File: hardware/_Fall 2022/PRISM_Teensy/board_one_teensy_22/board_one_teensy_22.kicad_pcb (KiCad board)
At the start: 2 copper layers, 15 parts, among them J1 EAST, J2 CORE_IO, J3 USB_micro, U1 Teensy4.1, U2 BNO055_Breakout, U3 3966

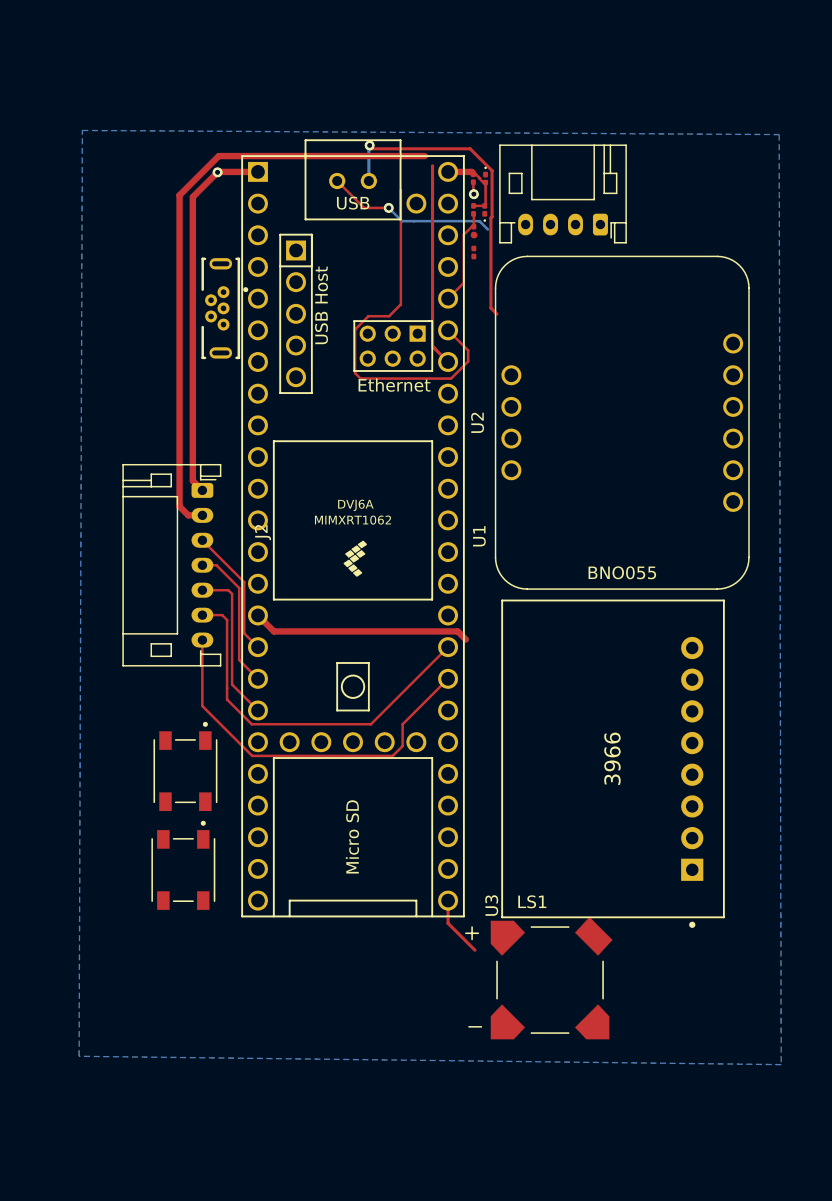
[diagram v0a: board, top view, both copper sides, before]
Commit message: Fix errors on TX/RX and added buzzer
Current state: Board 1 - need to check diodes; Board 4 - done; GPS- not showing layout traces, all need logos
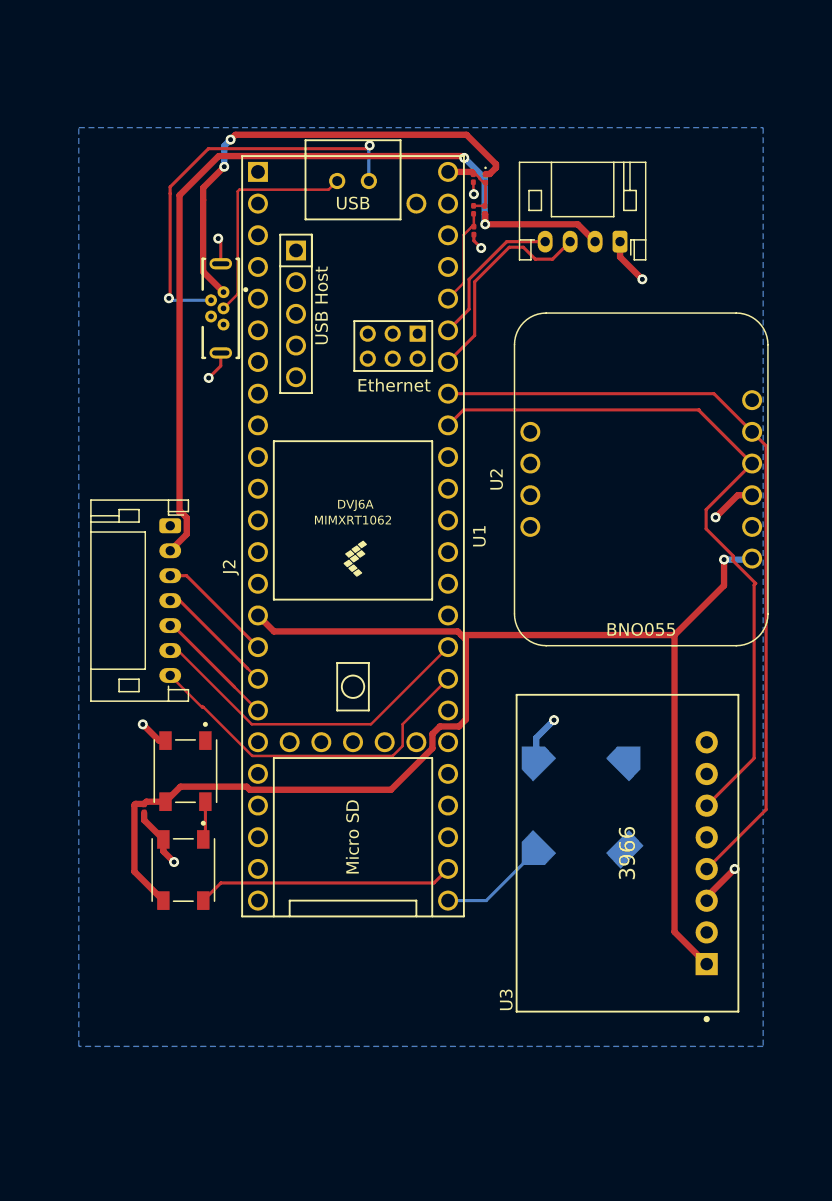
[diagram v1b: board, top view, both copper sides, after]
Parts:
- LS1: moved to B.Cu
- moved C2 51.8 mm to (115.7, 111.2), turned to 90 degrees
- moved LS1 14.2 mm to (150.8, 111.0)
- moved U3 7.65 mm to (154.5, 114.8)
- moved U2 4.79 mm to (155.6, 84.8)
- moved J2 3.83 mm to (117.8, 88.6)
- moved J1 2.08 mm to (153.9, 65.8)
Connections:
- C2 pad 2: +3.3V -> /3.3V
- D4 pad 3: +3.3V -> /3.3V
- D5 pad 3: +3.3V -> /3.3V
- U1 pad 42: /RX 0 -> /TX 0
- U1 pad 43: /TX 0 -> /RX 0
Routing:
- net /3.3V: track 17.5 -> 117.3 mm, vias 0 -> 1
- net /SCL 0: track 0.00 -> 63.1 mm
- net /SDA 0: track 0.00 -> 58.9 mm
- net /V_USB: track 0.00 -> 37.6 mm, vias 0 -> 2
- net /V_BATT: track 48.1 -> 69.8 mm, vias 0 -> 2
- net /NEOPIXEL: track 0.00 -> 20.7 mm
- net /TX 0: track 30.2 -> 17.1 mm
- net Net-(J3-Pad2): track 25.4 -> 32.9 mm, vias 1 -> 2
- net GND: track 30.9 -> 24.3 mm, vias 2 -> 8
- net Net-(J3-Pad3): track 13.7 -> 18.7 mm, vias 1 -> 0
- net unconnected-(J3-PadS1): track 0.00 -> 4.51 mm, vias 0 -> 2
- net /RX 0: track 16.2 -> 12.1 mm
- net /BUZZER: track 4.87 -> 8.72 mm
- net Net-(D4-Pad1): track 0.00 -> 3.10 mm
- net /ARM: track 12.7 -> 10.1 mm
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
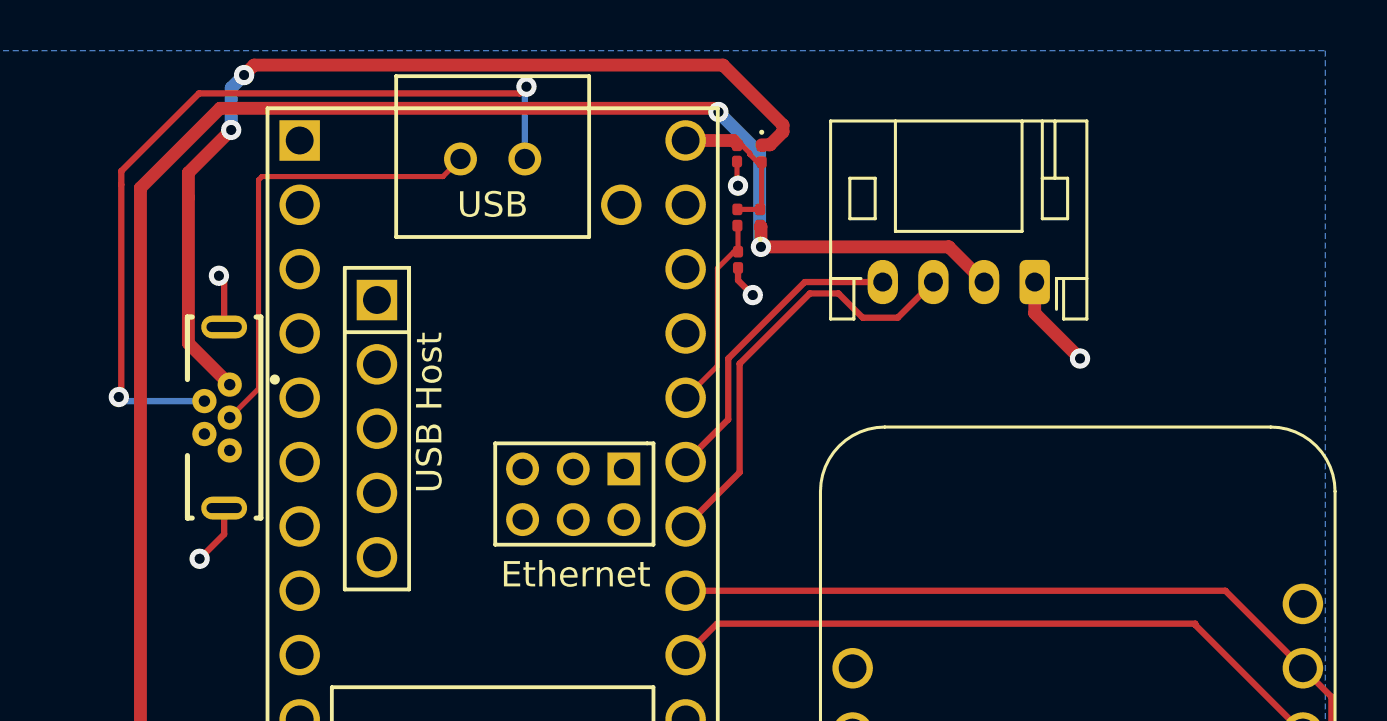
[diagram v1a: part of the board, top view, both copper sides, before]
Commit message: Add schottcky diodes to main teensy
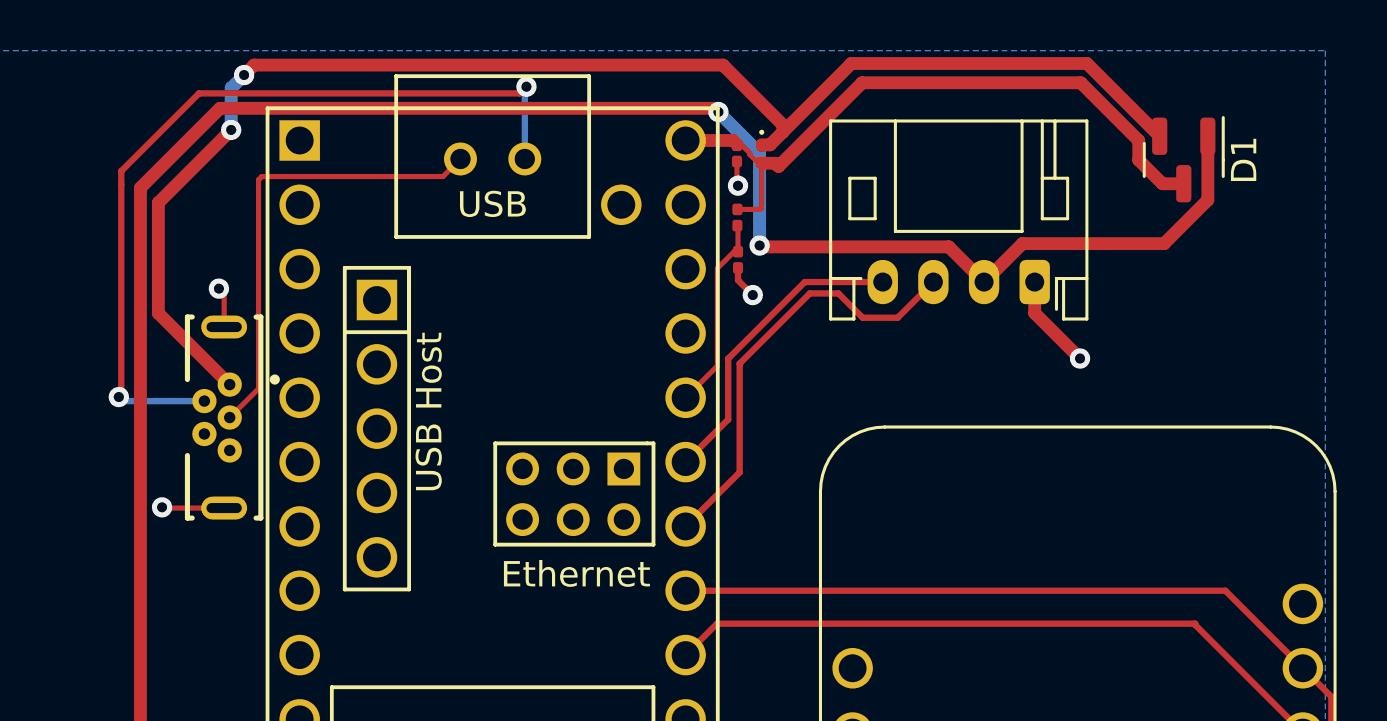
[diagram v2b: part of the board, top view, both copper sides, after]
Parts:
- D1: value DIODE -> BAT54C; footprint Diode_SMD:D_0201_0603Metric -> Package_TO_SOT_SMD:SOT-23
- R4: value 100K -> 200K
- moved D1 16.9 mm to (159.8, 61.0), turned to -90 degrees
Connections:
- D1 pad 2: /VIN -> /V_USB
- J3 pad S1: unconnected-(J3-PadS1) -> GND
- J3 pad S2: unconnected-(J3-PadS1) -> GND
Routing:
- net /VIN: track 6.16 -> 26.3 mm
- net /V_USB: track 37.6 -> 55.7 mm
- net /V_BATT: track 69.8 -> 81.7 mm
- net unconnected-(J3-PadS1): track 4.51 -> 0.00 mm, vias 2 -> 0
- net GND: track 24.3 -> 28.4 mm, vias 8 -> 10

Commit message: logos
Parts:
- added ?: LOGO, LOGO, F.Cu at (137.5, 53.6)
- added ?: LOGO, LOGO, F.Cu at (138.4, 134.6)
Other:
- board outline added: 61 x 88.9 mm

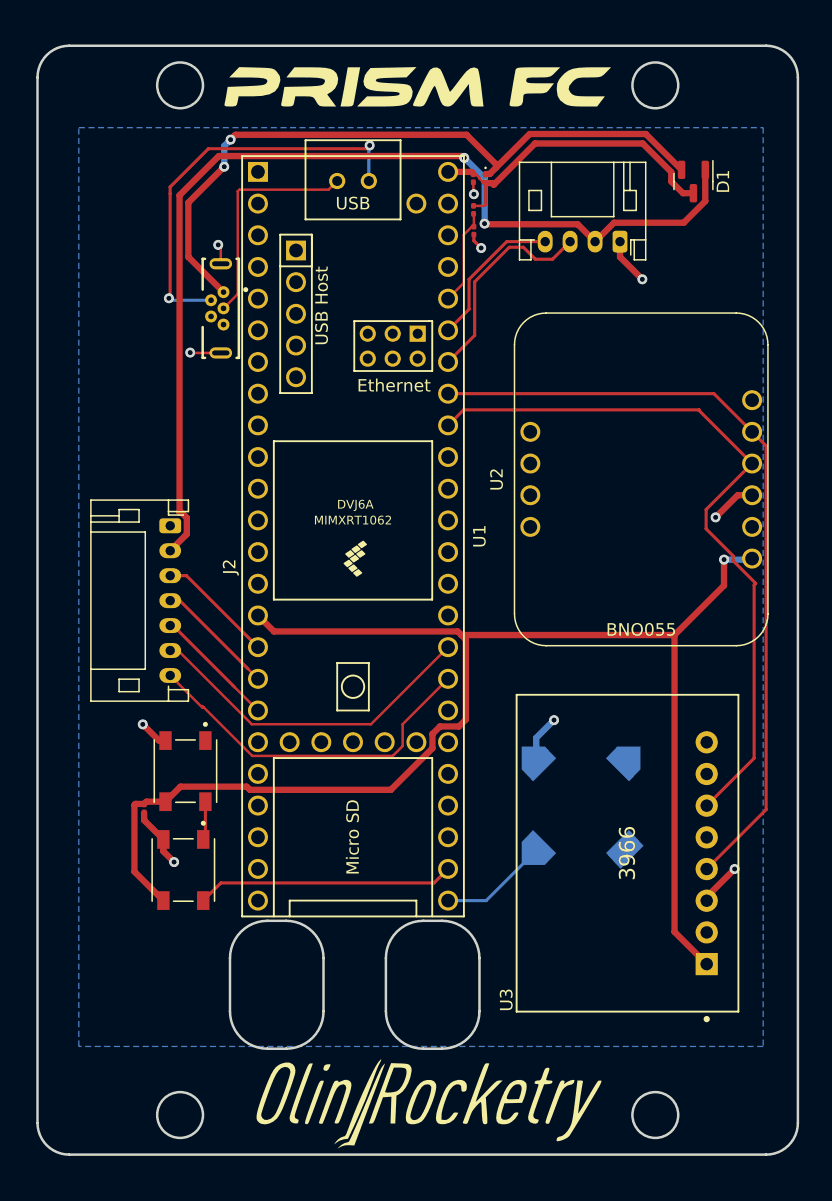
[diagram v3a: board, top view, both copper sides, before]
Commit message: Completed IO layout, added board 1 plated holes
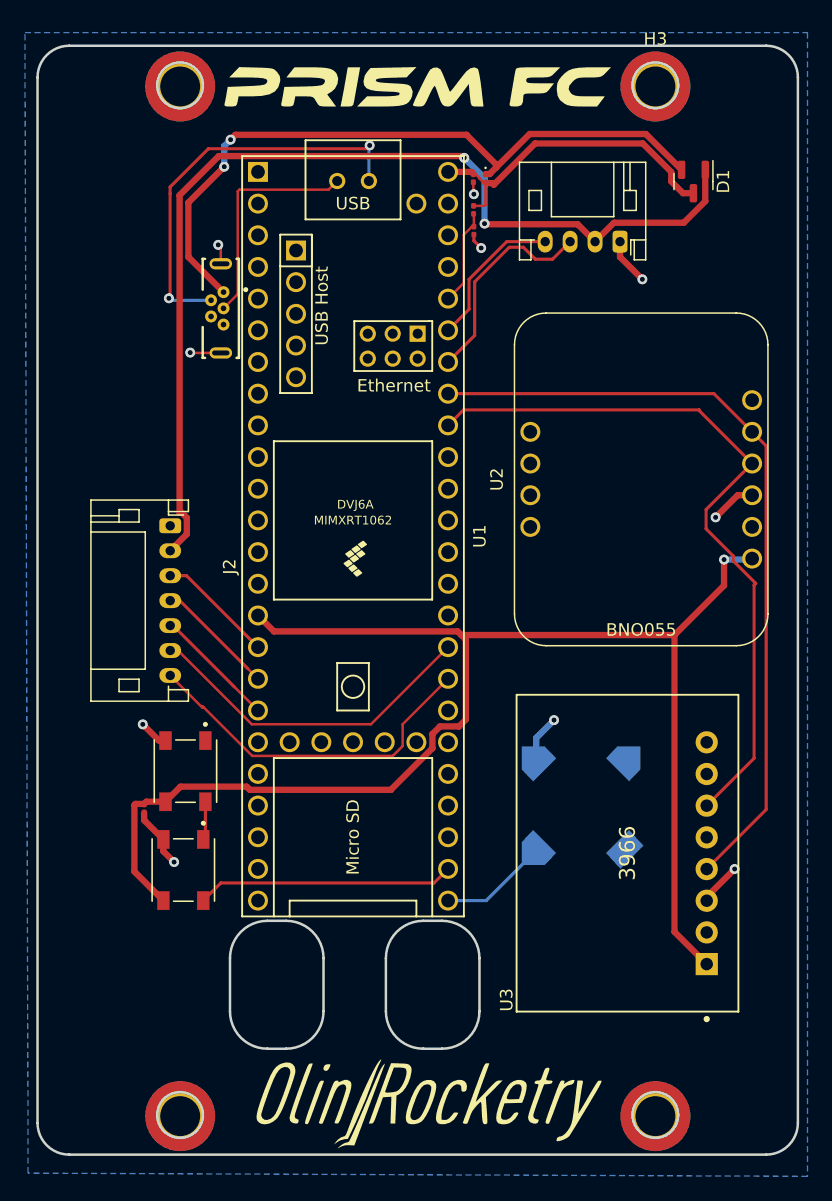
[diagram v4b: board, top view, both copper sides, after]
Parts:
- added H1: MountingHole_Pad, MountingHole:MountingHole_3.2mm_M3_DIN965_Pad_TopBottom, F.Cu at (118.6, 53.3)
- added H2: MountingHole, MountingHole:MountingHole_3.2mm_M3_DIN965_Pad_TopBottom, F.Cu at (156.7, 135.9)
- added H3: MountingHole, MountingHole:MountingHole_3.2mm_M3_DIN965_Pad_TopBottom, F.Cu at (156.7, 53.3)
- added H4: MountingHole, MountingHole:MountingHole_3.2mm_M3_DIN965_Pad_TopBottom, F.Cu at (118.6, 135.9)
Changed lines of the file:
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@@
     )
+  )
+  (footprint "MountingHole:MountingHole_3.2mm_M3_DIN965_Pad_TopBottom" (layer "F.Cu")
+    (at 118.618 53.34)
+    (descr "Mounting Hole 3.2mm, M3, DIN965")
+    (tags "mounting hole 3.2mm m3 din965")
+    (property "Sheetfile" "CoreIO.kicad_sch")
+    (property "Sheetname" "")
+    (attr exclude_from_pos_files)
+    (fp_text reference "H1" (at 0 -3.8) (layer "User.1")
+      (effects (font (size 1 1) (thickness 0.15)))
+    )
+    (fp_text value "MountingHole_Pad" (at 0 3.8) (layer "F.Fab")
+      (effects (font (size 1 1) (thickness 0.15)))
+    )
+    (fp_text user "${REFERENCE}" (at 0 0) (layer "F.Fab")
+      (effects (font (size 1 1) (thickness 0.15)))
+    )
+    (fp_circle (center 0 0) (end 2.8 0) (layer "Cmts.User") (width 0.15) (fill none))
+    (fp_circle (center 0 0) (end 3.05 0) (layer "F.CrtYd") (width 0.05) (fill none))
+    (pad "1" thru_hole circle (at 0 0) (size 3.6 3.6) (drill 3.2) (layers *.Cu *.Mask)
+      (pinfunction "1") (pintype "input"))
+    (pad "1" connect circle (at 0 0) (size 5.6 5.6) (layers "F.Cu" "F.Mask")
+      (pinfunction "1") (pintype "input"))
+    (pad "1" connect circle (at 0 0) (size 5.6 5.6) (layers "B.Cu" "B.Mask")
+      (pinfunction "1") (pintype "input"))
   )
   (footprint "neopixel:LED_1655" (layer "F.Cu")
@@
     )
   )
+  (footprint "MountingHole:MountingHole_3.2mm_M3_DIN965_Pad_TopBottom" (layer "F.Cu")
+    (at 118.618 135.89)
+    (descr "Mounting Hole 3.2mm, M3, DIN965")
+    (tags "mounting hole 3.2mm m3 din965")
+    (property "Sheetfile" "CoreIO.kicad_sch")
+    (property "Sheetname" "")
+    (attr exclude_from_pos_files)
+    (fp_text reference "H4" (at 0 -3.8) (layer "User.1")
+      (effects (font (size 1 1) (thickness 0.15)))
+    )
+    (fp_text value "MountingHole" (at 0 3.8) (layer "F.Fab")
+      (effects (font (size 1 1) (thickness 0.15)))
+    )
+    (fp_text user "${REFERENCE}" (at 0 0) (layer "F.Fab")
+      (effects (font (size 1 1) (thickness 0.15)))
+    )
+    (fp_circle (center 0 0) (end 2.8 0) (layer "Cmts.User") (width 0.15) (fill none))
+    (fp_circle (center 0 0) (end 3.05 0) (layer "F.CrtYd") (width 0.05) (fill none))
+    (pad "1" thru_hole circle (at 0 0) (size 3.6 3.6) (drill 3.2) (layers *.Cu *.Mask))
+    (pad "1" connect circle (at 0 0) (size 5.6 5.6) (layers "F.Cu" "F.Mask"))
+    (pad "1" connect circle (at 0 0) (size 5.6 5.6) (layers "B.Cu" "B.Mask"))
+  )
+  (footprint "MountingHole:MountingHole_3.2mm_M3_DIN965_Pad_TopBottom" (layer "F.Cu")
+    (at 156.718 53.34)
+    (descr "Mounting Hole 3.2mm, M3, DIN965")
+    (tags "mounting hole 3.2mm m3 din965")
+    (property "Sheetfile" "CoreIO.kicad_sch")
+    (property "Sheetname" "")
+    (attr exclude_from_pos_files)
+    (fp_text reference "H3" (at 0 -3.8) (layer "F.SilkS")
+      (effects (font (size 1 1) (thickness 0.15)))
+    )
+    (fp_text value "MountingHole" (at 0 3.8) (layer "F.Fab")
+      (effects (font (size 1 1) (thickness 0.15)))
+    )
+    (fp_text user "${REFERENCE}" (at 0 0) (layer "F.Fab")
+      (effects (font (size 1 1) (thickness 0.15)))
+    )
+    (fp_circle (center 0 0) (end 2.8 0) (layer "Cmts.User") (width 0.15) (fill none))
+    (fp_circle (center 0 0) (end 3.05 0) (layer "F.CrtYd") (width 0.05) (fill none))
+    (pad "1" thru_hole circle (at 0 0) (size 3.6 3.6) (drill 3.2) (layers *.Cu *.Mask))
+    (pad "1" connect circle (at 0 0) (size 5.6 5.6) (layers "B.Cu" "B.Mask"))
+    (pad "1" connect circle (at 0 0) (size 5.6 5.6) (layers "F.Cu" "F.Mask"))
+  )
   (footprint "Sensors:BNO055_Breakout" (layer "F.Cu")
     (at 155.58 84.84 90)
@@
       (rotate (xyz -90 0 0))
     )
+  )
+  (footprint "MountingHole:MountingHole_3.2mm_M3_DIN965_Pad_TopBottom" (layer "F.Cu")
+    (at 156.718 135.89)
+    (descr "Mounting Hole 3.2mm, M3, DIN965")
+    (tags "mounting hole 3.2mm m3 din965")
+    (property "Sheetfile" "CoreIO.kicad_sch")
+    (property "Sheetname" "")
+    (attr exclude_from_pos_files)
+    (fp_text reference "H2" (at 0 -3.8) (layer "User.1")
+      (effects (font (size 1 1) (thickness 0.15)))
+    )
+    (fp_text value "MountingHole" (at 0 3.8) (layer "F.Fab")
+      (effects (font (size 1 1) (thickness 0.15)))
+    )
+    (fp_text user "${REFERENCE}" (at 0 0) (layer "F.Fab")
+      (effects (font (size 1 1) (thickness 0.15)))
+    )
+    (fp_circle (center 0 0) (end 2.8 0) (layer "Cmts.User") (width 0.15) (fill none))
+    (fp_circle (center 0 0) (end 3.05 0) (layer "F.CrtYd") (width 0.05) (fill none))
+    (pad "1" thru_hole circle (at 0 0) (size 3.6 3.6) (drill 3.2) (layers *.Cu *.Mask))
+    (pad "1" connect circle (at 0 0) (size 5.6 5.6) (layers "B.Cu" "B.Mask"))
+    (pad "1" connect circle (at 0 0) (size 5.6 5.6) (layers "F.Cu" "F.Mask"))
   )
   (footprint "Diode_SMD:D_0201_0603Metric" (layer "F.Cu")
@@
     (polygon
       (pts
-        (xy 165.354 130.302)
-        (xy 110.49 130.302)
-        (xy 110.49 56.642)
-        (xy 165.354 56.642)
+        (xy 168.91 140.716)
+        (xy 106.426 140.462)
+        (xy 106.172 49.022)
+        (xy 168.91 49.022)
       )
     )

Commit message: Board one changed resistor size
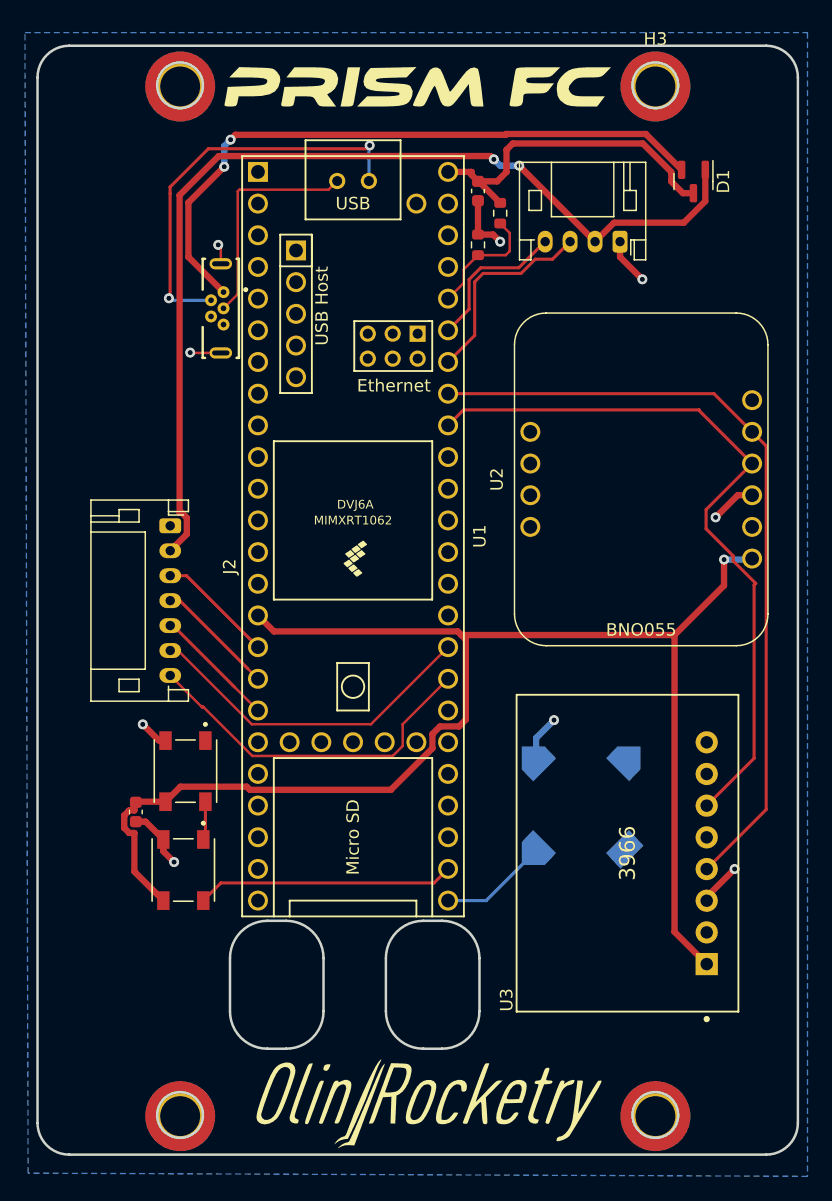
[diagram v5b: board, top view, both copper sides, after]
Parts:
- removed D2: DIODE, Diode_SMD:D_0201_0603Metric
- C1, C2: footprint Capacitor_SMD:C_0201_0603Metric -> Capacitor_SMD:C_0603_1608Metric
- R4, R5: footprint Resistor_SMD:R_0201_0603Metric -> Resistor_SMD:R_0603_1608Metric
- moved R4 2.15 mm to (144.3, 63.5)
- moved R5 1.19 mm to (142.5, 66.0), turned to 90 degrees
- moved C1 1.09 mm to (142.5, 61.7)
- moved C2 0.73 mm to (115.1, 111.5)
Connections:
- H1 pad 1: (no net) -> unconnected-(H1-Pad1)
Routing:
- net /V_USB: track 55.7 -> 52.3 mm
- net GND: track 28.4 -> 30.9 mm, vias 10 -> 9
- net /V_BATT: track 81.7 -> 79.5 mm
- net Net-(R4-Pad2): track 7.76 -> 9.69 mm
- net /3.3V: track 117.3 -> 118.4 mm
- net /TX 0: track 17.1 -> 16.3 mm
- net /VIN: track 26.3 -> 27.0 mm
